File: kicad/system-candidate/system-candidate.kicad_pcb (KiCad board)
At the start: 4 copper layers, 154 x 81 mm, 269 parts, among them J1 691137710002 2P 5.00mm, J2 Auxiliary 12V, J3 Differential audio, J301 T1_SECONDARY, J4 Control 2x4: 3V3 RESET FAULT 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, J401 START_BUTTON, J5 B2P-VH(LF)(SN), J6 GND braid solder bond - NO mo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, J7 B7B-XH-A(LF)(SN), J8 FAN 12V, K501 G6K-2F DC12, Q501 MMBT3904, Q502 MMBT3904, Q601 BCP56, Q602 BCP53, Q603 BSS138, Q701 BSS138, Q702 BSS138, Q703 BSS138, Q704 BSS138, Q705 BSS138, Q706 BSS138, Q707 AO3400A, U1 TPA3255DDV, U2 OPA1656ID, U3 OPA1656ID, U302 LM5164DDA, U303 TPS3700DDC, U401 LP2985-33, U402 TPS3808G33, U403 TPS3808G33, U404 TPS3808G33, U405 74LVC1G14, U406 74LVC2G74, U407 74LVC2G74, U408 74LVC1G32, U409 74LVC1G07, U410 74LVC1G08, U411 74LVC1G06, U412 TPS3700DDC, U413 TPS3700DDC, U414 TPS3808G33, U415 74LVC1G08, U416 TPS3808G33, U417 74LVC2G74, U418 74LVC1G32, U419 74LVC1G07, U501 TPS3700DDC, U502 TPS3700DDC, U503 TMUX6219, U504 TPS3700DDC

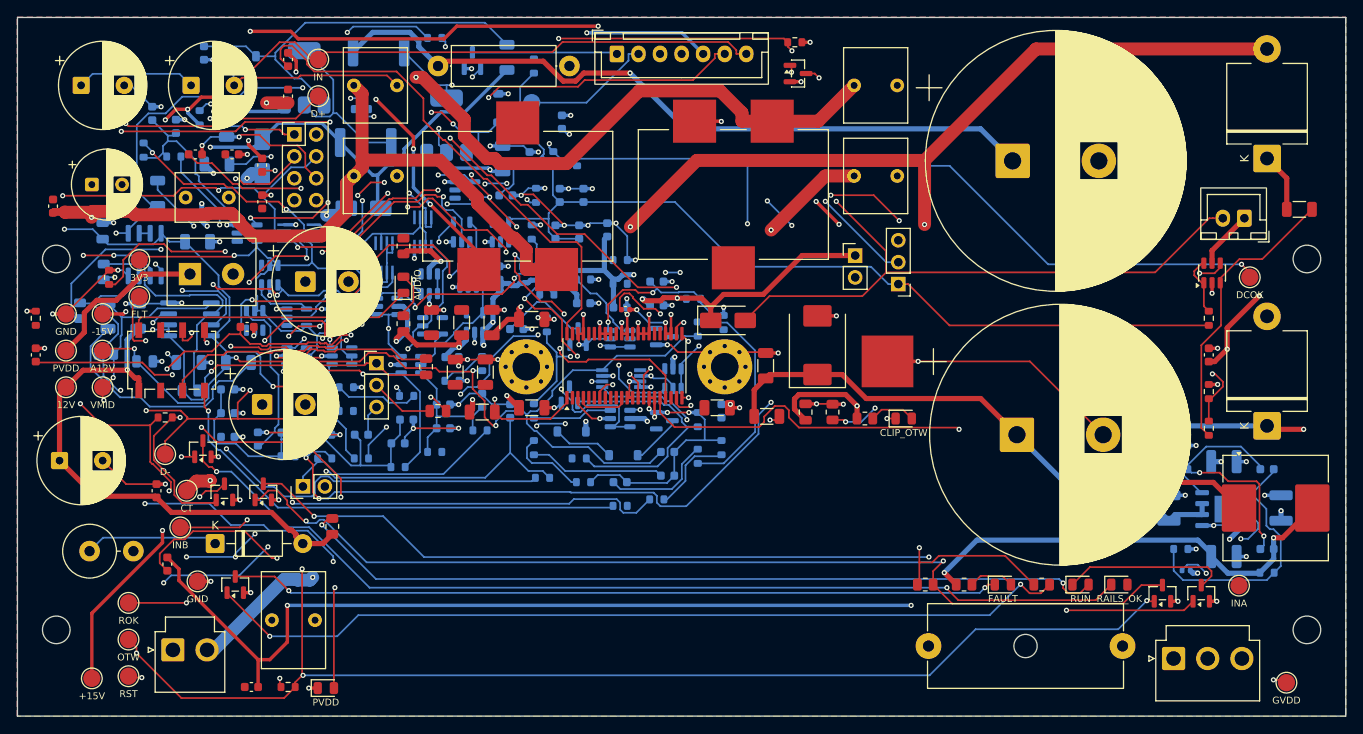
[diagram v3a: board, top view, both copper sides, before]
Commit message: feat(pcb): segunda passada de rota e GND sólido em pads THT
- route_system_candidate.py --resume: mantém o cobre e liga só o que falta
- fills GND externos com conexão sólida (sem starved_thermal)
- 3.073 trilhas, 407 vias; ERC 0, DRC 0 violações, paridade 0
- 58 conexões abertas (15 no U1) registradas em PCB-002
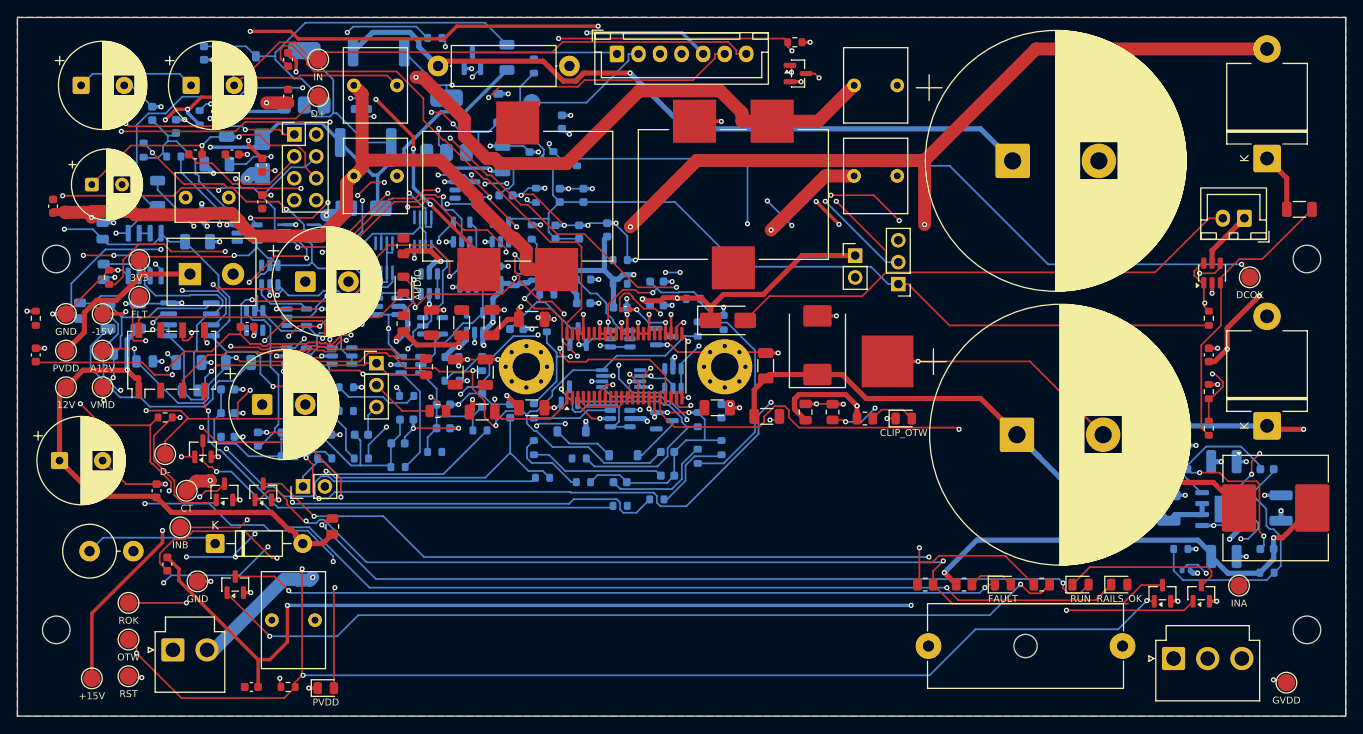
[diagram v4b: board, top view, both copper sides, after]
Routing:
- net /RAILS_OK: track 163.4 -> 195.0 mm, vias 9 -> 12
- net /GND: track 927.4 -> 949.2 mm
- net /PVDD: track 391.1 -> 396.5 mm
- net /LED705_A: track 5.36 -> 6.78 mm
- net /LED_ROK_K: track 115.2 -> 116.5 mm
- net /CLIP_N: track 155.3 -> 156.1 mm
- net /AUX_RAW: track 416.6 -> 417.4 mm
- net /LED706_A: track 5.37 -> 6.10 mm
- net /FAULT_N: track 124.1 -> 124.8 mm
